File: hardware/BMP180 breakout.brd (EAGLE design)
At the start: 15.2 x 15.2 mm, 15 parts, among them U1 BMP180

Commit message: Review for reds
Minor updates to PCB, updated library and example code, added datasheet
and readme
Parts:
- removed LOGO3: LOGO-SFESK, SparkFun-Aesthetics:SFE-LOGO-FLAME
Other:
- board text added: "BARO"
- board text added: "V10"
- board text removed: "V02"
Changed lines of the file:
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@@
 <setting verticaltext="up"/>
 </settings>
-<grid distance="0.05" unitdist="inch" unit="inch" style="lines" multiple="2" display="yes" altdistance="0.0125" altunitdist="inch" altunit="inch"/>
+<grid distance="0.05" unitdist="inch" unit="inch" style="lines" multiple="2" display="yes" altdistance="0.00625" altunitdist="inch" altunit="inch"/>
 <layers>
 <layer number="1" name="Top" color="4" fill="1" visible="yes" active="yes"/>
@@
 <layer number="20" name="Dimension" color="15" fill="1" visible="yes" active="yes"/>
 <layer number="21" name="tPlace" color="16" fill="1" visible="yes" active="yes"/>
-<layer number="22" name="bPlace" color="14" fill="1" visible="no" active="yes"/>
+<layer number="22" name="bPlace" color="14" fill="1" visible="yes" active="yes"/>
 <layer number="23" name="tOrigins" color="15" fill="1" visible="no" active="yes"/>
-<layer number="24" name="bOrigins" color="15" fill="1" visible="no" active="yes"/>
+<layer number="24" name="bOrigins" color="15" fill="1" visible="yes" active="yes"/>
 <layer number="25" name="tNames" color="7" fill="1" visible="no" active="yes"/>
 <layer number="26" name="bNames" color="7" fill="1" visible="no" active="yes"/>
 <layer number="27" name="tValues" color="7" fill="1" visible="no" active="yes"/>
 <layer number="28" name="bValues" color="7" fill="1" visible="no" active="yes"/>
-<layer number="29" name="tStop" color="7" fill="3" visible="no" active="yes"/>
+<layer number="29" name="tStop" color="7" fill="3" visible="yes" active="yes"/>
 <layer number="30" name="bStop" color="7" fill="6" visible="no" active="yes"/>
 <layer number="31" name="tCream" color="7" fill="4" visible="no" active="yes"/>
@@
 <layer number="37" name="tTest" color="7" fill="1" visible="no" active="yes"/>
 <layer number="38" name="bTest" color="7" fill="1" visible="no" active="yes"/>
-<layer number="39" name="tKeepout" color="4" fill="11" visible="no" active="yes"/>
+<layer number="39" name="tKeepout" color="4" fill="11" visible="yes" active="yes"/>
 <layer number="40" name="bKeepout" color="1" fill="11" visible="no" active="yes"/>
 <layer number="41" name="tRestrict" color="4" fill="10" visible="no" active="yes"/>
@@
 <wire x1="15.24" y1="15.24" x2="0" y2="15.24" width="0.2032" layer="20"/>
 <wire x1="0" y1="15.24" x2="0" y2="0" width="0.2032" layer="20"/>
-<text x="4.2545" y="13.6525" size="1.27" layer="21" font="vector" ratio="15">BMP180</text>
-<text x="4.60375" y="2.2225" size="1.27" layer="21" font="vector" ratio="15">+</text>
-<text x="1.905" y="2.38125" size="1.016" layer="21" font="vector" ratio="15">IO</text>
-<text x="7.14375" y="2.2225" size="1.27" layer="21" font="vector" ratio="15">-</text>
-<text x="9.36625" y="2.38125" size="1.016" layer="21" font="vector" ratio="15">CL</text>
-<text x="11.90625" y="2.38125" size="1.016" layer="21" font="vector" ratio="15">DA</text>
-<text x="10.95375" y="13.6525" size="1.27" layer="22" font="vector" ratio="15" rot="MR0">BMP180</text>
+<text x="7.77875" y="13.335" size="1.27" layer="21" font="vector" ratio="15" align="bottom-center">BMP180</text>
+<text x="4.60375" y="2.2225" size="1.27" layer="21" font="vector" ratio="20">+</text>
+<text x="1.905" y="2.38125" size="1.016" layer="21" font="vector" ratio="20">IO</text>
+<text x="7.14375" y="2.2225" size="1.27" layer="21" font="vector" ratio="20">-</text>
+<text x="9.36625" y="2.38125" size="1.016" layer="21" font="vector" ratio="20">CL</text>
+<text x="11.90625" y="2.38125" size="1.016" layer="21" font="vector" ratio="20">DA</text>
+<text x="7.46125" y="13.335" size="1.27" layer="22" font="vector" ratio="15" rot="MR0" align="bottom-center">BMP180</text>
 <text x="12.065" y="2.54" size="1.27" layer="22" font="vector" ratio="15" rot="MR90">SDA</text>
 <text x="9.525" y="2.54" size="1.27" layer="22" font="vector" ratio="15" rot="MR90">SCL</text>
@@
 <text x="6.35" y="-10.16" size="1.778" layer="27" font="vector">M Grusin</text>
 <dimension x1="2.54" y1="1.27" x2="2.54" y2="12.7" x3="-1.27" y3="6.985" textsize="1.016" textratio="10" layer="47" dtype="vertical" unit="inch"/>
-<text x="0.381" y="0.3175" size="1.016" layer="16" font="vector" ratio="15" rot="MR90">V02</text>
+<text x="0.381" y="0.3175" size="1.016" layer="16" font="vector" ratio="20" rot="MR90">V10</text>
+<text x="7.77875" y="11.7475" size="1.27" layer="21" font="vector" ratio="15" align="bottom-center">BARO</text>
+<text x="7.46125" y="11.7475" size="1.27" layer="22" font="vector" ratio="15" rot="MR0" align="bottom-center">BARO</text>
 </plain>
 <attributes>
@@
 <element name="LOGO1" library="SparkFun-Aesthetics" package="SFE-NEW-WEB" value="LOGO-SFENW2" x="13.97" y="7.9375" rot="MR0"/>
 <element name="LOGO2" library="SparkFun-Aesthetics" package="OSHW-LOGO-S" value="OSHW-LOGOS" x="7.62" y="7.14375" rot="MR0"/>
-<element name="LOGO3" library="SparkFun-Aesthetics" package="SFE-LOGO-FLAME" value="LOGO-SFESK" x="6.985" y="10.63625" rot="MR0"/>
 <element name="STANDOFF1" library="SparkFun-Electromechanical" package="STAND-OFF" value="STAND-OFF" x="12.7" y="12.7"/>
 <element name="STANDOFF2" library="SparkFun-Electromechanical" package="STAND-OFF" value="STAND-OFF" x="2.54" y="12.7"/>
@@
 </polygon>
 <via x="10.4775" y="7.62" extent="1-16" drill="0.508"/>
-<via x="8.5725" y="12.7" extent="1-16" drill="0.508"/>
+<via x="9.8425" y="11.1125" extent="1-16" drill="0.508"/>
 <via x="0.9525" y="9.8425" extent="1-16" drill="0.508"/>
 </signal>

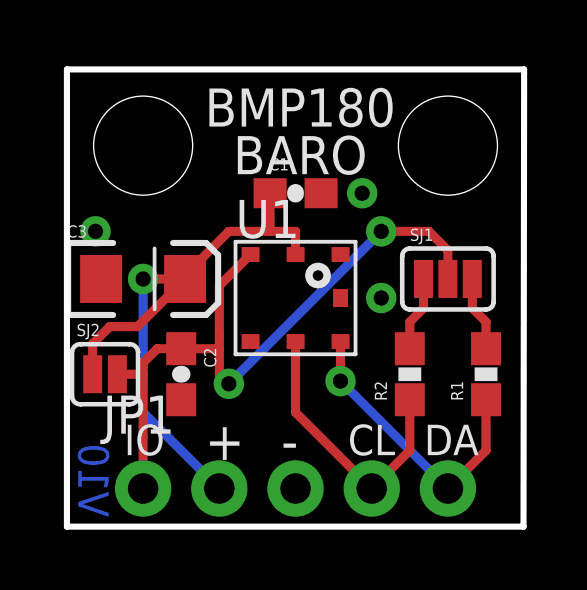
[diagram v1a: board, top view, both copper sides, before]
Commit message: Minor changes for reds (V10)
Added silk to solder jumpers
Added BMP180 part to SparkFun Eagle Libraries
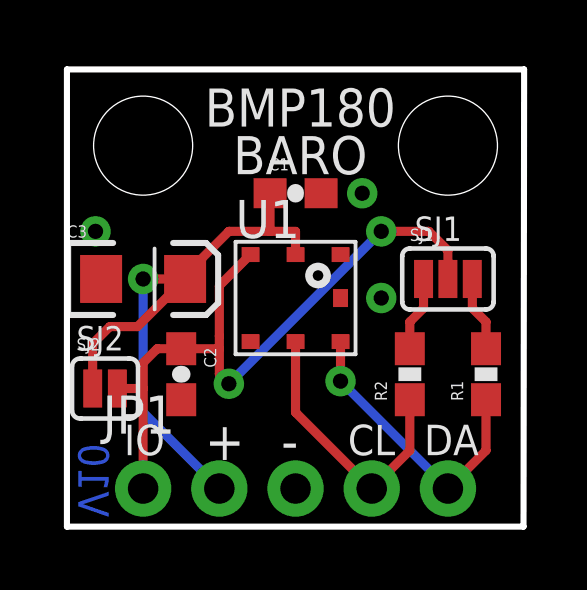
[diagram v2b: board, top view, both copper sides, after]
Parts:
- U1: device mike-temp:BMP180 -> SparkFun-Sensors:BMP180
- moved SJ2 0.48 mm to (1.27, 4.60)
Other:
- board text added: "SJ1"
- board text added: "SJ2"

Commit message: Added microfiducials
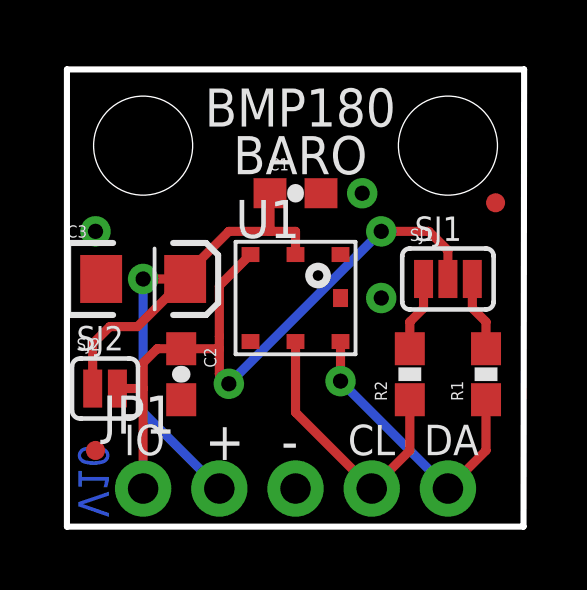
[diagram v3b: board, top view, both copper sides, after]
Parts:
- added FID1, FID2: FIDUCIALUFIDUCIAL, SparkFun-Aesthetics:MICRO-FIDUCIAL
